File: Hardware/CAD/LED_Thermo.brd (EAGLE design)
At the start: 54.9 x 55 mm, 41 parts, among them IC1 MEGA48/88/168-AU, IC2 MAX481CSA, J1 USB_Micro, Q2 KERAMIKRESONATOR_CSTCC_16MHZ

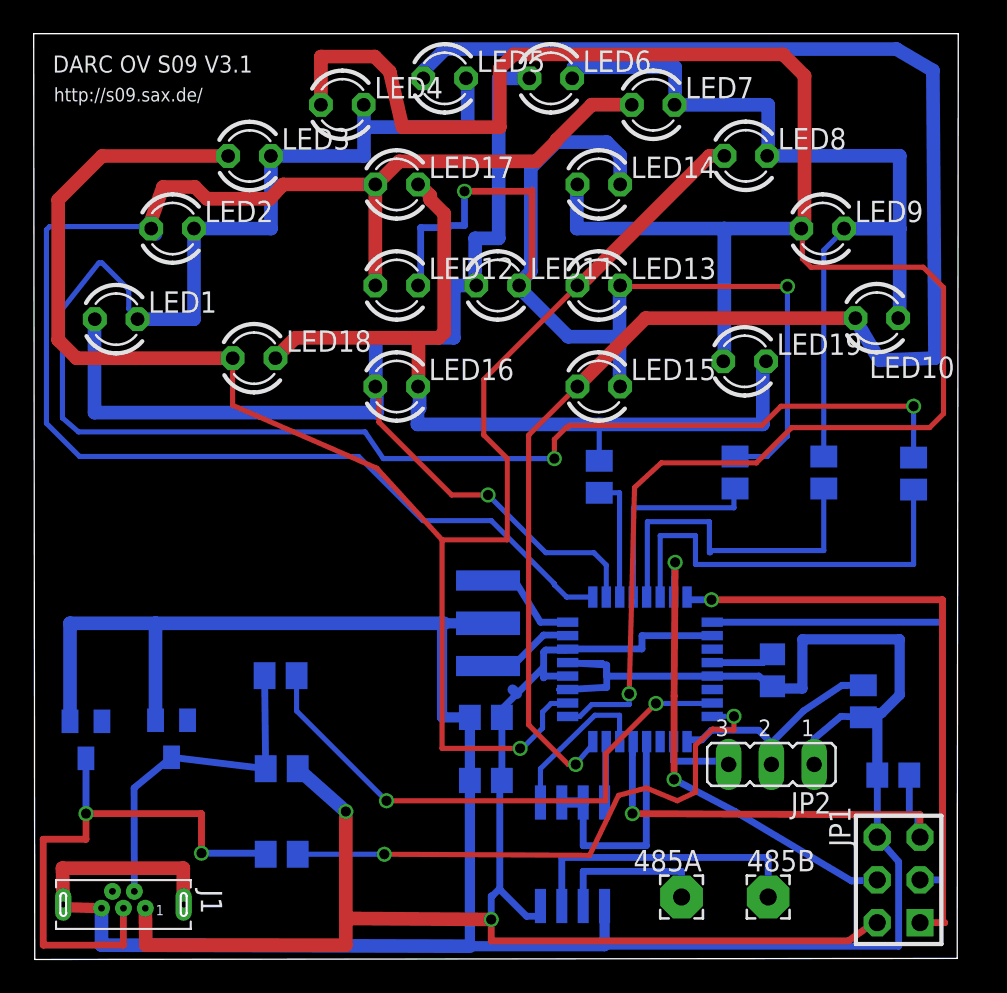
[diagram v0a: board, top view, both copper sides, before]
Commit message: Sicherung eingefuegt, Gerberdateien aktualisiert
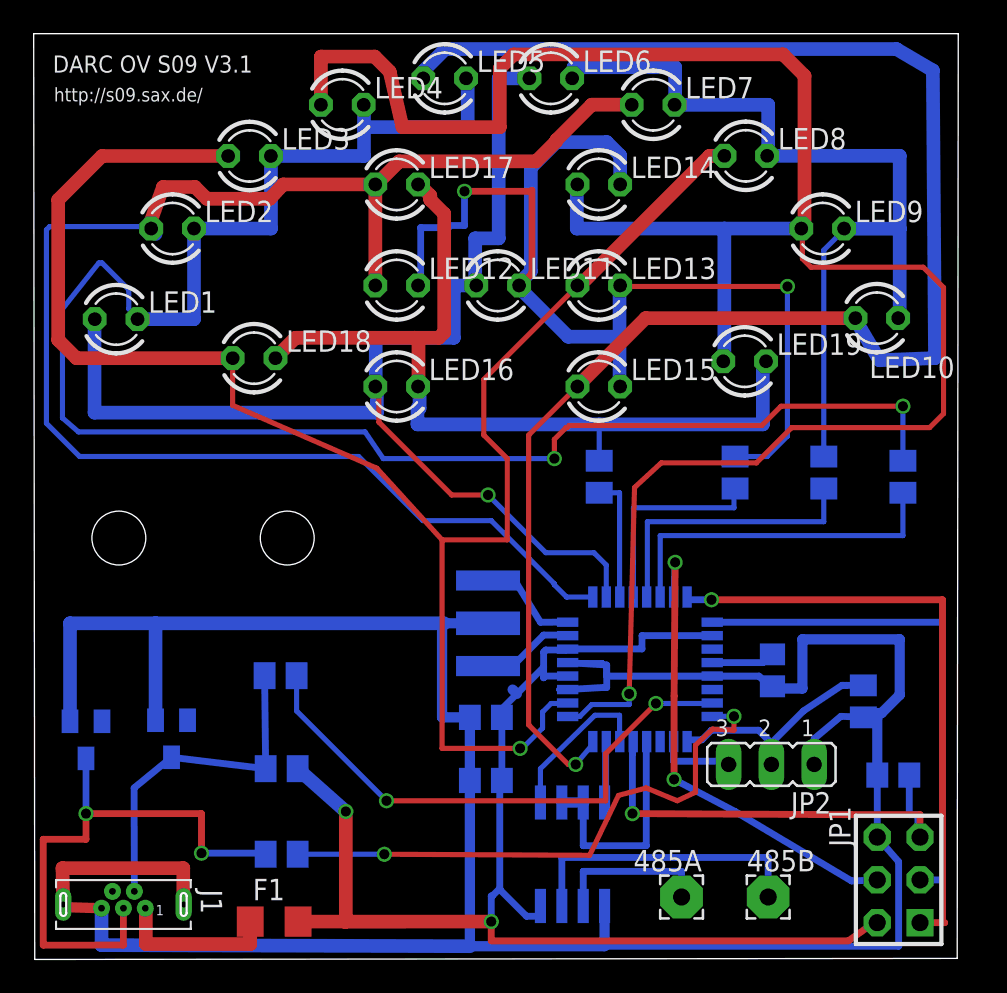
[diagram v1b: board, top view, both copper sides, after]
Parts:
- added F1: FUSE, fuse:FUSE_1206
- moved R10 0.66 mm to (51.6, 28.6)
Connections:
- new net N$4: F1.1, J1.1
- net VCC: now also F1.2; no longer J1.1
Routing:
- net VCC: track 93.7 -> 81.2 mm
- net N$4: track 0.00 -> 9.69 mm
- net N$22: track 24.9 -> 20.6 mm
- net N$19: track 20.6 -> 17.0 mm
- net N$14: track 106.7 -> 106.0 mm
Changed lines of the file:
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@@
 <text x="1.0795" y="52.6415" size="1.016" layer="25">DARC OV S09 V3.1</text>
 <text x="1.143" y="50.927" size="0.8128" layer="25">http://s09.sax.de/</text>
+<hole x="5" y="25" drill="3.2"/>
+<hole x="15" y="25" drill="3.2"/>
 </plain>
 <attributes>
@@
 </class>
 </classes>
-<designrules name="multi_pcb *">
-<description language="en">&lt;b&gt;EAGLE Design Rules&lt;/b&gt;
+<designrules name="multi_pcb">
+<description language="de">&lt;b&gt;EAGLE Design Rules&lt;/b&gt;
 &lt;p&gt;
 Design Regel Lötstopmaske wird über die Vias gelegt für Multi pcb</description>
@@
 <element name="R8" library="rcl" package="M0805" value="390" x="41.5925" y="28.8925" rot="MR90"/>
 <element name="R9" library="rcl" package="M0805" value="390" x="46.863" y="28.8925" rot="MR90"/>
-<element name="R10" library="rcl" package="M0805" value="390" x="52.197" y="28.829" rot="MR90"/>
+<element name="R10" library="rcl" package="M0805" value="390" x="51.562" y="28.6385" rot="MR90"/>
 <element name="C8" library="rcl" package="C0805" value="100nF" x="50.9905" y="10.922" rot="MR180"/>
 <element name="C9" library="rcl" package="C0805" value="100nF" x="26.797" y="10.6045" rot="MR180"/>
@@
 <attribute name="VALUE" x="0.7894" y="5.109" size="1.27" layer="27" font="vector" ratio="13" rot="SR0"/>
 </element>
+<element name="F1" library="fuse" package="FUSE_1206" value="FUSE" x="14.224" y="2.2225"/>
 </elements>
 <signals>
@@
 <wire x1="29.21" y1="2.54" x2="29.9085" y2="2.54" width="0.4064" layer="16"/>
 <wire x1="29.9085" y1="2.54" x2="30.0355" y2="2.667" width="0.4064" layer="16"/>
-<wire x1="27.1145" y1="2.3495" x2="27.1145" y2="1.0795" width="0.4064" layer="1"/>
-<wire x1="27.1145" y1="3.7465" x2="27.1145" y2="2.3495" width="0.4064" layer="16"/>
+<wire x1="27.1145" y1="2.2225" x2="27.1145" y2="1.0795" width="0.4064" layer="1"/>
+<wire x1="27.1145" y1="3.7465" x2="27.1145" y2="2.2225" width="0.4064" layer="16"/>
 <wire x1="27.178" y1="3.7465" x2="27.1145" y2="3.7465" width="0.4064" layer="16"/>
 <wire x1="27.6225" y1="4.191" x2="27.178" y2="3.7465" width="0.4064" layer="16"/>
 <wire x1="28.3845" y1="16.002" x2="28.6385" y2="15.748" width="0.6096" layer="16"/>
-<via x="27.1145" y="2.3495" extent="1-16" drill="0.6" shape="square"/>
-<contactref element="J1" pad="1"/>
+<via x="27.1145" y="2.2225" extent="1-16" drill="0.6" shape="square"/>
 <wire x1="15.6185" y1="11.303" x2="18.4785" y2="8.763" width="0.8128" layer="16"/>
 <via x="18.4785" y="8.763" extent="1-16" drill="0.6"/>
 <wire x1="18.4785" y1="8.763" x2="18.4785" y2="2.4765" width="0.8128" layer="1"/>
-<wire x1="18.4785" y1="2.4765" x2="18.482059375" y2="2.410290625" width="0.8128" layer="1"/>
-<wire x1="18.482059375" y1="2.410290625" x2="27.1145" y2="2.3495" width="0.8128" layer="1"/>
-<wire x1="6.5705" y1="3.0185" x2="6.604" y2="0.8255" width="0.8128" layer="1"/>
-<wire x1="6.604" y1="0.8255" x2="18.4785" y2="0.8255" width="0.8128" layer="1"/>
-<wire x1="18.4785" y1="0.8255" x2="18.482059375" y2="2.410290625" width="0.8128" layer="1"/>
+<wire x1="18.4785" y1="2.4765" x2="18.418559375" y2="2.219790625" width="0.8128" layer="1"/>
+<wire x1="18.418559375" y1="2.219790625" x2="27.1145" y2="2.2225" width="0.8128" layer="1"/>
+<contactref element="F1" pad="2"/>
+<wire x1="18.48149375" y1="2.221353125" x2="18.418559375" y2="2.219790625" width="0.8128" layer="1"/>
+<wire x1="15.646" y1="2.2225" x2="18.48149375" y2="2.2225" width="0.8128" layer="1"/>
+<wire x1="18.48149375" y1="2.2225" x2="18.48149375" y2="2.221353125" width="0.8128" layer="1"/>
 </signal>
 <signal name="N$2">
@@
 <wire x1="19.558" y1="50.73" x2="19.54" y2="50.73" width="0.8128" layer="16"/>
 <wire x1="14.03" y1="47.69" x2="19.558" y2="47.69" width="0.8128" layer="16"/>
-<wire x1="19.558" y1="47.69" x2="19.558" y2="49.149" width="0.8128" layer="16"/>
-<wire x1="19.558" y1="49.149" x2="19.558" y2="50.73" width="0.8128" layer="16"/>
+<wire x1="19.558" y1="47.69" x2="19.558" y2="49.403" width="0.8128" layer="16"/>
+<wire x1="19.558" y1="49.403" x2="19.558" y2="50.73" width="0.8128" layer="16"/>
 <wire x1="25.7175" y1="52.3" x2="25.62" y2="52.3" width="0.8128" layer="16"/>
 <wire x1="25.7175" y1="49.403" x2="25.7175" y2="52.3" width="0.8128" layer="16"/>
 <wire x1="19.558" y1="49.403" x2="25.7175" y2="49.403" width="0.8128" layer="16"/>
-<wire x1="19.558" y1="49.149" x2="19.558" y2="49.403" width="0.8128" layer="16"/>
-<wire x1="52.197" y1="32.8295" x2="52.197" y2="29.779" width="0.3048" layer="16"/>
-<wire x1="44.323" y1="32.8295" x2="52.197" y2="32.8295" width="0.3048" layer="1"/>
+<wire x1="51.562" y1="32.8295" x2="51.562" y2="29.5885" width="0.3048" layer="16"/>
+<wire x1="44.323" y1="32.8295" x2="51.562" y2="32.8295" width="0.3048" layer="1"/>
 <wire x1="43.18" y1="31.6865" x2="44.323" y2="32.8295" width="0.3048" layer="1"/>
 <wire x1="31.75" y1="31.6865" x2="43.18" y2="31.6865" width="0.3048" layer="1"/>
@@
 <wire x1="5.588" y1="39.751" x2="5.588" y2="38.608" width="0.3048" layer="16"/>
 <wire x1="5.588" y1="38.608" x2="6.1595" y2="38.0365" width="0.3048" layer="16"/>
-<via x="52.197" y="32.8295" extent="1-16" drill="0.6" shape="square"/>
+<via x="51.562" y="32.8295" extent="1-16" drill="0.6" shape="square"/>
 <via x="30.861" y="29.718" extent="1-16" drill="0.6" shape="square"/>
 </signal>
@@
 <contactref element="R10" pad="1"/>
 <contactref element="IC1" pad="14"/>
-<wire x1="52.197" y1="23.4315" x2="52.197" y2="27.879" width="0.3048" layer="16"/>
-<wire x1="39.243" y1="23.4315" x2="52.197" y2="23.4315" width="0.3048" layer="16"/>
-<wire x1="39.243" y1="25.146" x2="39.243" y2="23.4315" width="0.3048" layer="16"/>
+<wire x1="51.562" y1="25.146" x2="51.562" y2="27.6885" width="0.3048" layer="16"/>
+<wire x1="37.1475" y1="25.146" x2="51.562" y2="25.146" width="0.3048" layer="16"/>
 <wire x1="37.1455" y1="21.4966" x2="37.1475" y2="21.4966" width="0.3048" layer="16"/>
-<wire x1="37.1475" y1="25.146" x2="39.243" y2="25.146" width="0.3048" layer="16"/>
 <wire x1="37.1475" y1="21.4966" x2="37.1475" y2="25.146" width="0.3048" layer="16"/>
 </signal>
@@
 <contactref element="IC1" pad="13"/>
 <contactref element="R9" pad="1"/>
-<wire x1="46.863" y1="24.257" x2="46.863" y2="27.9425" width="0.3048" layer="16"/>
-<wire x1="40.132" y1="24.257" x2="46.863" y2="24.257" width="0.3048" layer="16"/>
-<wire x1="40.132" y1="24.13" x2="40.132" y2="24.257" width="0.3048" layer="16"/>
-<wire x1="40.0685" y1="24.13" x2="40.132" y2="24.13" width="0.3048" layer="16"/>
-<wire x1="40.0685" y1="25.9715" x2="40.0685" y2="24.13" width="0.3048" layer="16"/>
 <wire x1="36.3455" y1="21.4966" x2="36.3855" y2="21.4966" width="0.3048" layer="16"/>
-<wire x1="36.3855" y1="25.9715" x2="40.0685" y2="25.9715" width="0.3048" layer="16"/>
 <wire x1="36.3855" y1="21.4966" x2="36.3855" y2="25.9715" width="0.3048" layer="16"/>
+<wire x1="36.3855" y1="25.9715" x2="46.863" y2="25.9715" width="0.3048" layer="16"/>
+<wire x1="46.863" y1="25.9715" x2="46.863" y2="27.9425" width="0.3048" layer="16"/>
 </signal>
 <signal name="N$18">
@@
 <wire x1="13.7185" y1="11.303" x2="13.655" y2="16.8275" width="0.4064" layer="16"/>
 </signal>
+<signal name="N$4">
+<contactref element="J1" pad="1"/>
+<contactref element="F1" pad="1"/>
+<wire x1="6.5705" y1="3.0185" x2="6.604" y2="3.0185" width="0.8128" layer="1"/>
+<wire x1="6.604" y1="3.0185" x2="6.604" y2="0.889" width="0.8128" layer="1"/>
+<wire x1="6.604" y1="0.889" x2="12.802" y2="0.889" width="0.8128" layer="1"/>
+<wire x1="12.802" y1="0.889" x2="12.802" y2="2.2225" width="0.8128" layer="1"/>
+</signal>
 </signals>

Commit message: Taster eingefuegt, Gerberdateien ueberarbeitet
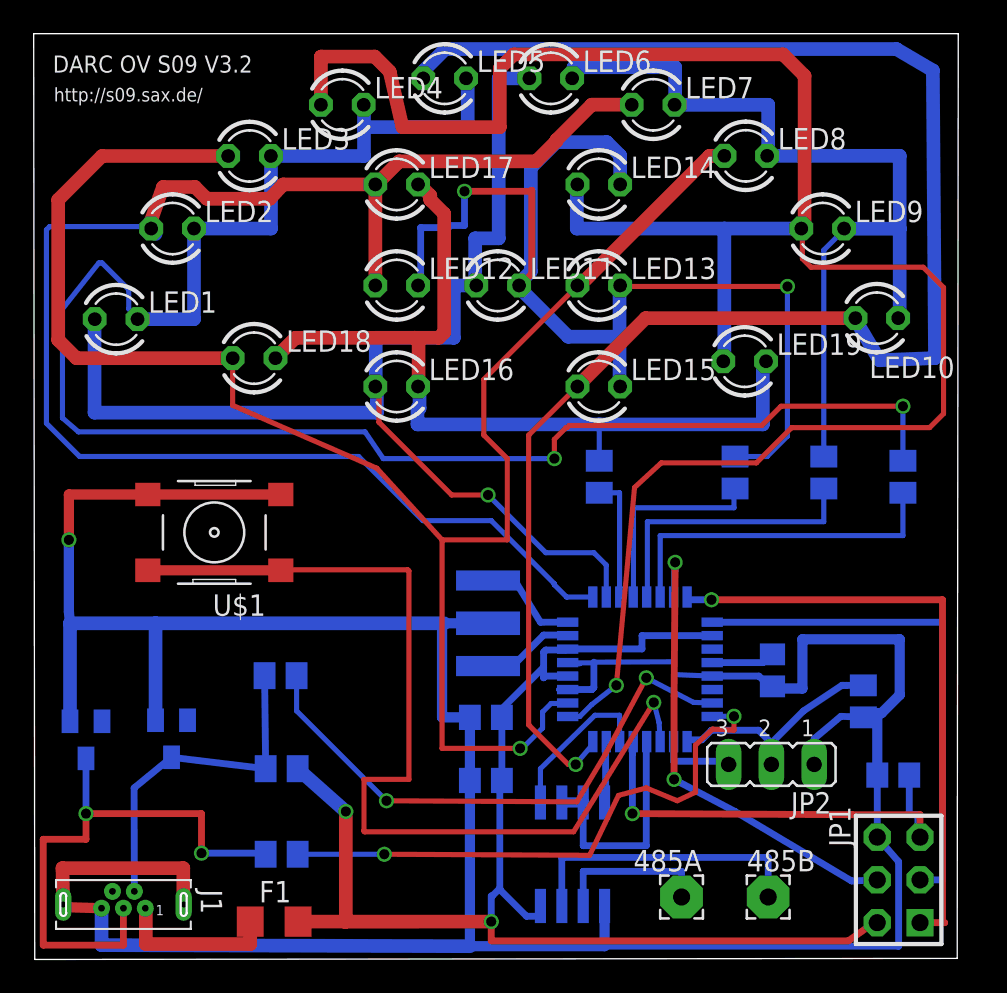
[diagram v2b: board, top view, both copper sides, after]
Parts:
- added U$1: B3FS-1002, switch-omron:B3FS-1002
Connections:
- new net N$6: IC1.27, U$1.P$3, U$1.P$4
- net GND: now also U$1.P$1, U$1.P$2
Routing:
- net N$6: track 0.00 -> 57.6 mm, vias 0 -> 1
- net GND: track 190.0 -> 199.1 mm, vias 0 -> 1
- net N$12: track 127.8 -> 126.4 mm
- net N$1: track 33.0 -> 33.7 mm
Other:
- board text added: "DARC OV S09 V3.2"
- board text removed: "DARC OV S09 V3.1"

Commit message: USB-Schutzschaltung,12MHZ Quarz integriert,Layout + Loetstopmake optimiert
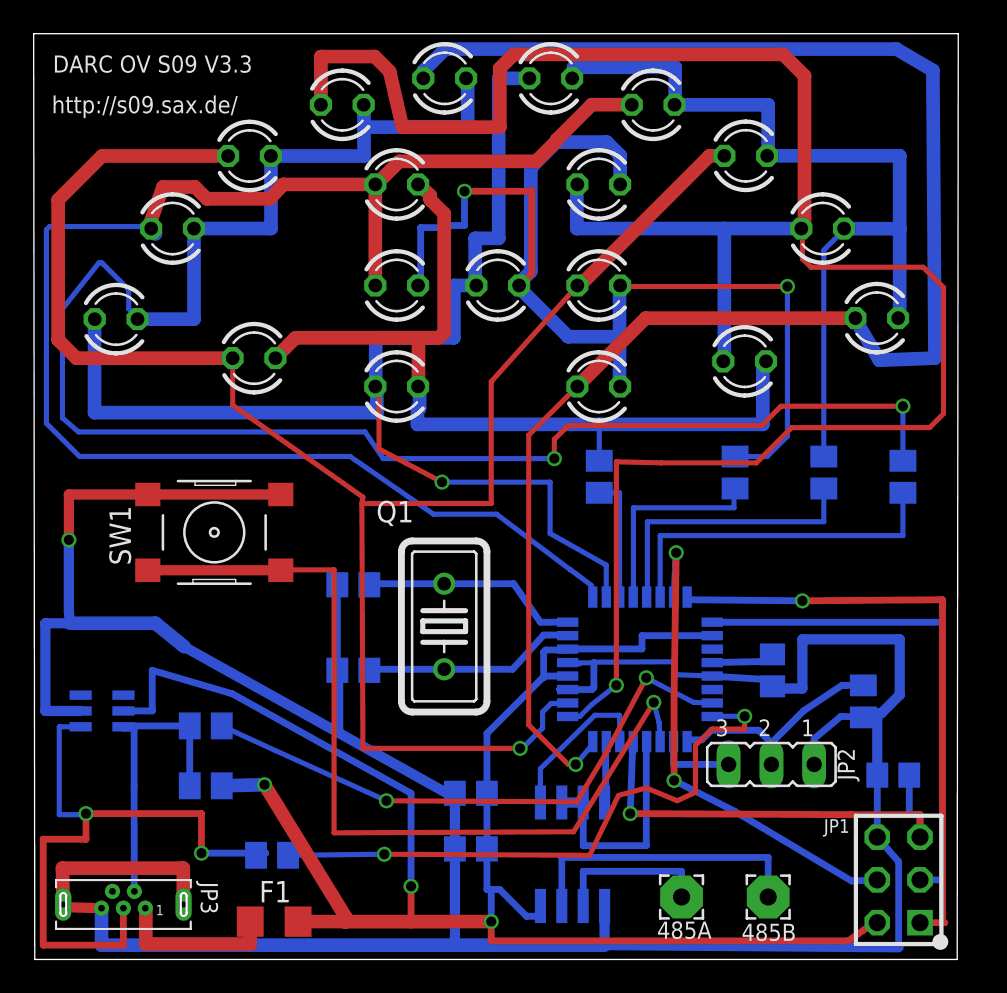
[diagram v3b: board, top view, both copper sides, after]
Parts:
- removed D1: ZD 3,6, diode:SOT23
- removed D2: ZD3,6, diode:SOT23
- removed Q2: KERAMIKRESONATOR_CSTCC_16MHZ, atmel:CSTCC
- added C1, C2: 22pF, rcl:C0805
- added IC3: IP4220CZ6, IP4220CZ6:SOT95P275X110-6N
- added Q1: 12MHZ, crystal:HC18U-V
- 485A: value RS485A -> (+)
- 485B: value RS485B -> B(-)
- IC1: value MEGA48/88/168-AU -> MEGA68-AU
- moved R1 5.35 mm to (10.2, 13.8)
- moved R3 4.62 mm to (10.2, 10.3)
- moved C12 4.60 mm to (25.9, 9.84)
- moved C9 4.16 mm to (25.9, 6.54)
- moved R2 0.58 mm to (14.1, 6.16)
- renumbered J1 to JP3, U$1 to SW1
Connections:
- net GND: now also C1.1, C2.1, IC3.2; no longer D1.1, D2.1, Q2.SMD2
- net N$24: now also C1.2, Q1.2; no longer Q2.SMD1
- net N$25: now also C2.2, Q1.1; no longer Q2.SMD3
- net N$7: now also IC3.1; no longer D1.3
- net N$8: now also IC3.6; no longer D2.3
- net VCC: now also IC3.5
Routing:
- net VCC: track 80.9 -> 112.8 mm, vias 2 -> 3
- net N$24: track 5.56 -> 12.8 mm
- net N$25: track 6.11 -> 13.0 mm
- net N$7: track 33.7 -> 39.1 mm
- net N$6: track 57.6 -> 52.3 mm
- net GND: track 199.1 -> 194.1 mm
- net N$8: track 20.2 -> 17.4 mm
- net N$9: track 103.7 -> 106.1 mm
- net N$2: track 73.0 -> 75.1 mm
- net N$12: track 126.4 -> 128.4 mm
- net N$3: track 33.8 -> 35.5 mm
- net N$17: track 28.7 -> 29.9 mm
- net N$1: track 33.7 -> 34.8 mm
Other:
- outline, holes or cut-outs redrawn
- board text added: "DARC OV S09 V3.3"
- board text removed: "DARC OV S09 V3.2"
